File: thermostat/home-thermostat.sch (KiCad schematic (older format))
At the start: 53 parts, among them J1 Amphenol_132289 SMA, J4 Conn_ARM_JTAG_SWD_10, U1 MKW41Z512VHT, U10 SN74LVC2T45DCUR, U9 SN74LVC2T45DCUR, Y1 32MHz 10PPM SMT 2.0x1.6mm 10PF, Y2 32.768KHz 20PPM 3.2x1.5mm 7PF

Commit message: Fine grouping of parts done, may start routing . GPIO connector on wrong side of PCB (I wanted to have the buttons on the opposite side, but thats not a big problem.
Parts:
- removed TP13: UART_TX, TestPoint:TestPoint_Pad_D1.0mm, symbol Connector:TestPoint
- removed TP16: UART_RX, TestPoint:TestPoint_Pad_D1.0mm, symbol Connector:TestPoint
- added J7: Thermosthat, Connector_PinHeader_2.54mm:PinHeader_1x03_P2.54mm_Vertical_SMD_Pin1Left, symbol Connector_Generic:Conn_01x03
- C14, C29, C46, C47, C48, C56, C57, C58, C59: footprint Capacitor_SMD:C_0603_1608Metric -> Capacitor_SMD:C_0402_1005Metric
- R2: footprint Resistor_SMD:R_0603_1608Metric -> Resistor_SMD:R_0402_1005Metric
- U1: footprint Package_DFN_QFN:NXP_LQFN-48-1EP_7x7mm_P0.5mm_EP3.5x3.5mm_16xMask0.45x0.45_ThermalVias -> Package_DFN_QFN:NXP_LQFN-48-1EP_7x7mm_P0.5mm_EP3.5x3.5mm_16xMask0.45x0.45
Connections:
- net BTN_OK: now also U1.41 (PTC5)
- net GND: now also J7.3 (Pin_3)
- net UART_TX: now reaches U9.7 (B1)
- net UART_TX: now also J7.1 (Pin_1)
- net UART_RX: now reaches U10.7 (B1)
- net UART_RX: now also J7.2 (Pin_2)
- no-connect marks 18 -> 17
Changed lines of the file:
@@
 F 0 "C14" H -935 1996 50  0000 L CNN
 F 1 "1n" H -935 1905 50  0000 L CNN
-F 2 "Capacitor_SMD:C_0603_1608Metric" H -1012 1800 50  0001 C CNN
+F 2 "Capacitor_SMD:C_0402_1005Metric" H -1012 1800 50  0001 C CNN
 F 3 "~" H -1050 1950 50  0001 C CNN
 	1    -1050 1950
@@
 F 0 "R2" H -1120 1404 50  0000 R CNN
 F 1 "0" H -1120 1495 50  0000 R CNN
-F 2 "Resistor_SMD:R_0603_1608Metric" V -1120 1450 50  0001 C CNN
+F 2 "Resistor_SMD:R_0402_1005Metric" V -1120 1450 50  0001 C CNN
 F 3 "~" H -1050 1450 50  0001 C CNN
 	1    -1050 1450
@@
 F1 "gpio.sch" 50
 F2 "BTN_OK" I L 12650 3400 50
-F3 "BTN_CANCEL" I L 12650 3500 50
-F4 "LED_OUT" I L 12650 3600 50
-F5 "LED_RED" I L 12650 3700 50
-F6 "LED_GREEN" I L 12650 3800 50
-F7 "SCL" I L 12650 3000 50
-F8 "SDA" I L 12650 3100 50
-F9 "~INT" I L 12650 3200 50
-F10 "BTN_RST" I L 12650 3300 50
+F3 "LED_OUT" I L 12650 3600 50
+F4 "LED_RED" I L 12650 3700 50
+F5 "LED_GREEN" I L 12650 3800 50
+F6 "SCL" I L 12650 3000 50
+F7 "SDA" I L 12650 3100 50
+F8 "~INT" I L 12650 3200 50
+F9 "BTN_RST" I L 12650 3300 50
 $EndSheet
 Text Label 8200 3150 2    50   ~ 0
@@
 Text Label 12150 3400 0    50   ~ 0
 BTN_OK
-Text Label 12150 3500 0    50   ~ 0
-BTN_CANCEL
 Wire Wire Line
 	12150 3400 12650 3400
-Wire Wire Line
-	12150 3500 12650 3500
 Wire Wire Line
 	8200 2550 7650 2550
@@
 F 0 "U1" H 6000 5800 50  0000 C CNN
 F 1 "MKW41Z512VHT" H 7600 5800 50  0000 C CNN
-F 2 "Package_DFN_QFN:NXP_LQFN-48-1EP_7x7mm_P0.5mm_EP3.5x3.5mm_16xMask0.45x0.45_ThermalVias" H 6700 4050 50  0001 C CNN
+F 2 "Package_DFN_QFN:NXP_LQFN-48-1EP_7x7mm_P0.5mm_EP3.5x3.5mm_16xMask0.45x0.45" H 6700 4050 50  0001 C CNN
 F 3 "https://www.nxp.com/docs/en/data-sheet/MKW41Z512.pdf" H 6750 3950 50  0001 C CNN
 	1    6750 4050
@@
 $EndComp
 NoConn ~ 7650 2850
-NoConn ~ 7650 2950
 NoConn ~ 7650 3350
 NoConn ~ 7650 3950
@@
 F 0 "C46" H -2135 4996 50  0000 L CNN
 F 1 "1u" H -2135 4905 50  0000 L CNN
-F 2 "Capacitor_SMD:C_0603_1608Metric" H -2212 4800 50  0001 C CNN
+F 2 "Capacitor_SMD:C_0402_1005Metric" H -2212 4800 50  0001 C CNN
 F 3 "~" H -2250 4950 50  0001 C CNN
 	1    -2250 4950
@@
 F 0 "C47" H -1035 4996 50  0000 L CNN
 F 1 "1u" H -1035 4905 50  0000 L CNN
-F 2 "Capacitor_SMD:C_0603_1608Metric" H -1112 4800 50  0001 C CNN
+F 2 "Capacitor_SMD:C_0402_1005Metric" H -1112 4800 50  0001 C CNN
 F 3 "~" H -1150 4950 50  0001 C CNN
 	1    -1150 4950
@@
 F 0 "C48" H -685 4996 50  0000 L CNN
 F 1 "0,1u" H -685 4905 50  0000 L CNN
-F 2 "Capacitor_SMD:C_0603_1608Metric" H -762 4800 50  0001 C CNN
+F 2 "Capacitor_SMD:C_0402_1005Metric" H -762 4800 50  0001 C CNN
 F 3 "~" H -800 4950 50  0001 C CNN
 	1    -800 4950
@@
 F 0 "C29" H -2535 4996 50  0000 L CNN
 F 1 "0,1u" H -2535 4905 50  0000 L CNN
-F 2 "Capacitor_SMD:C_0603_1608Metric" H -2612 4800 50  0001 C CNN
+F 2 "Capacitor_SMD:C_0402_1005Metric" H -2612 4800 50  0001 C CNN
 F 3 "~" H -2650 4950 50  0001 C CNN
 	1    -2650 4950
@@
 Wire Wire Line
 	-2750 5650 -2100 5650
-$Comp
-L Connector:TestPoint TP13
-U 1 1 5F7FA6AE
-P -1000 5650
-F 0 "TP13" V -805 5722 50  0000 C CNN
-F 1 "UART_TX" V -896 5722 50  0000 C CNN
-F 2 "TestPoint:TestPoint_Pad_D1.0mm" H -800 5650 50  0001 C CNN
-F 3 "~" H -800 5650 50  0001 C CNN
-	1    -1000 5650
-	0    1    1    0
-$EndComp
 Wire Wire Line
 	-1000 5650 -1300 5650
@@
 F 0 "C57" H -2135 7196 50  0000 L CNN
 F 1 "1u" H -2135 7105 50  0000 L CNN
-F 2 "Capacitor_SMD:C_0603_1608Metric" H -2212 7000 50  0001 C CNN
+F 2 "Capacitor_SMD:C_0402_1005Metric" H -2212 7000 50  0001 C CNN
 F 3 "~" H -2250 7150 50  0001 C CNN
 	1    -2250 7150
@@
 F 0 "C58" H -1035 7196 50  0000 L CNN
 F 1 "1u" H -1035 7105 50  0000 L CNN
-F 2 "Capacitor_SMD:C_0603_1608Metric" H -1112 7000 50  0001 C CNN
+F 2 "Capacitor_SMD:C_0402_1005Metric" H -1112 7000 50  0001 C CNN
 F 3 "~" H -1150 7150 50  0001 C CNN
 	1    -1150 7150
@@
 F 0 "C59" H -685 7196 50  0000 L CNN
 F 1 "0,1u" H -685 7105 50  0000 L CNN
-F 2 "Capacitor_SMD:C_0603_1608Metric" H -762 7000 50  0001 C CNN
+F 2 "Capacitor_SMD:C_0402_1005Metric" H -762 7000 50  0001 C CNN
 F 3 "~" H -800 7150 50  0001 C CNN
 	1    -800 7150
@@
 F 0 "C56" H -2535 7196 50  0000 L CNN
 F 1 "0,1u" H -2535 7105 50  0000 L CNN
-F 2 "Capacitor_SMD:C_0603_1608Metric" H -2612 7000 50  0001 C CNN
+F 2 "Capacitor_SMD:C_0402_1005Metric" H -2612 7000 50  0001 C CNN
 F 3 "~" H -2650 7150 50  0001 C CNN
 	1    -2650 7150
@@
 	-350 6950 -800 6950
 Connection ~ -800 6950
-$Comp
-L Connector:TestPoint TP16
-U 1 1 5F8612B7
-P -1000 7850
-F 0 "TP16" V -805 7922 50  0000 C CNN
-F 1 "UART_RX" V -896 7922 50  0000 C CNN
-F 2 "TestPoint:TestPoint_Pad_D1.0mm" H -800 7850 50  0001 C CNN
-F 3 "~" H -800 7850 50  0001 C CNN
-	1    -1000 7850
-	0    1    1    0
-$EndComp
 Wire Wire Line
 	-1800 6950 -1800 7450
@@
 	-1050 1750 -1050 1800
 Connection ~ -1050 1750
+$Comp
+L Connector_Generic:Conn_01x03 J7
+U 1 1 5FA1C616
+P 1600 6900
+AR Path="/5FA1C616" Ref="J7"  Part="1"
+AR Path="/5E6A63AE/5FA1C616" Ref="J?"  Part="1"
+F 0 "J7" H 1680 6942 50  0000 L CNN
+F 1 "Thermosthat" H 1680 6851 50  0000 L CNN
+F 2 "Connector_PinHeader_2.54mm:PinHeader_1x03_P2.54mm_Vertical_SMD_Pin1Left" H 1600 6900 50  0001 C CNN
+F 3 "~" H 1600 6900 50  0001 C CNN
+	1    1600 6900
+	1    0    0    -1
+$EndComp
+Text Label -1000 5650 2    50   ~ 0
+UART_TX
+Text Label -1000 7850 2    50   ~ 0
+UART_RX
+$Comp
+L power:GND #PWR?
+U 1 1 5FA2E08F
+P 1350 7050
+AR Path="/5E8AC4D3/5FA2E08F" Ref="#PWR?"  Part="1"
+AR Path="/5FA2E08F" Ref="#PWR0114"  Part="1"
+F 0 "#PWR0114" H 1350 6800 50  0001 C CNN
+F 1 "GND" H 1355 6877 50  0000 C CNN
+F 2 "" H 1350 7050 50  0001 C CNN
+F 3 "" H 1350 7050 50  0001 C CNN
+	1    1350 7050
+	1    0    0    -1
+$EndComp
+Wire Wire Line
+	1350 7050 1350 7000
+Wire Wire Line
+	1350 7000 1400 7000
+Text Label 1050 6900 0    50   ~ 0
+UART_RX
+Text Label 1050 6800 0    50   ~ 0
+UART_TX
+Wire Wire Line
+	1050 6800 1400 6800
+Wire Wire Line
+	1050 6900 1400 6900
+Text Label 8200 2950 2    50   ~ 0
+BTN_OK
+Wire Wire Line
+	8200 2950 7650 2950
 $EndSCHEMATC

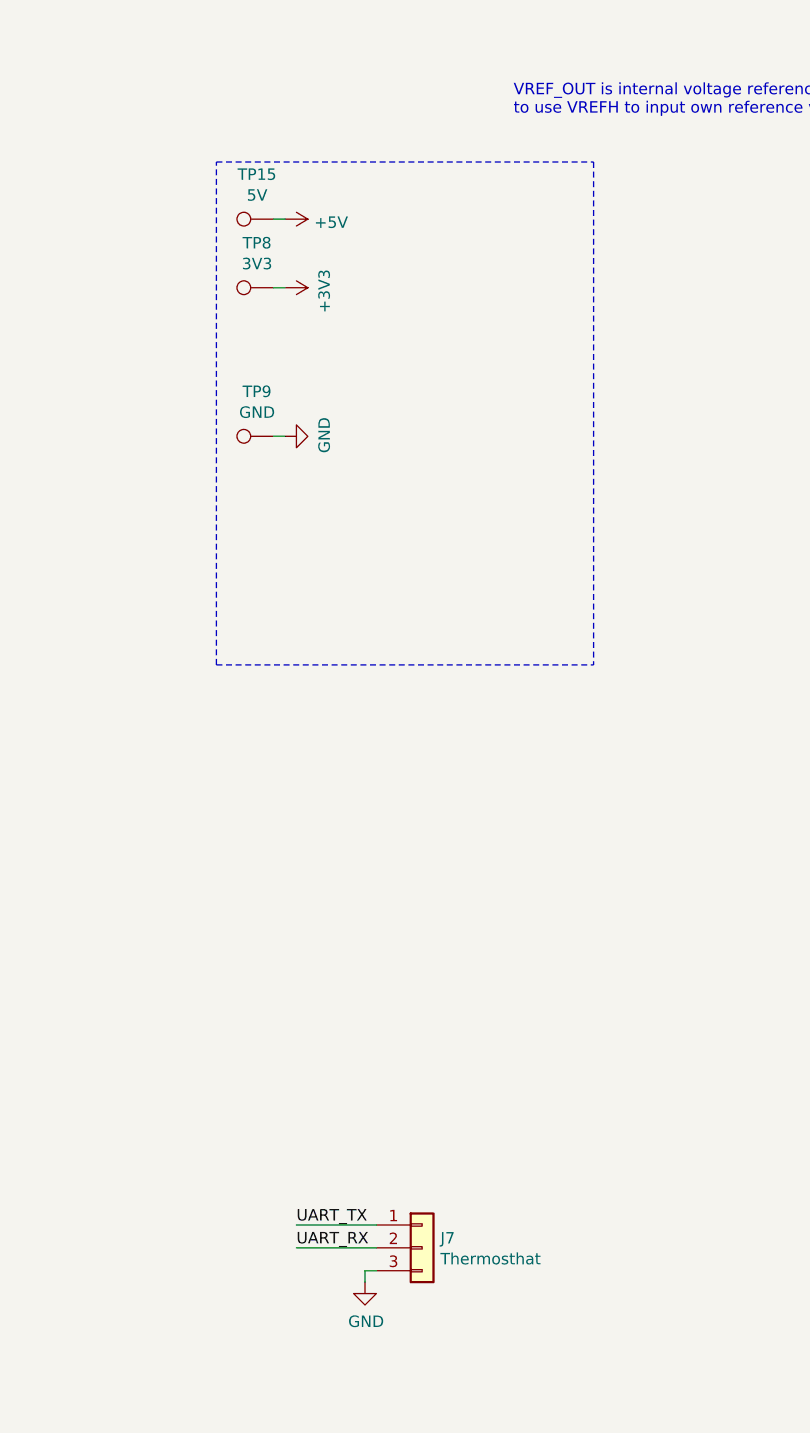
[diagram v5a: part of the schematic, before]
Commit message: Changed LED and regulator_out drivers to NMOS instead of bipolar. Started routing, SPI and I2C lines done.
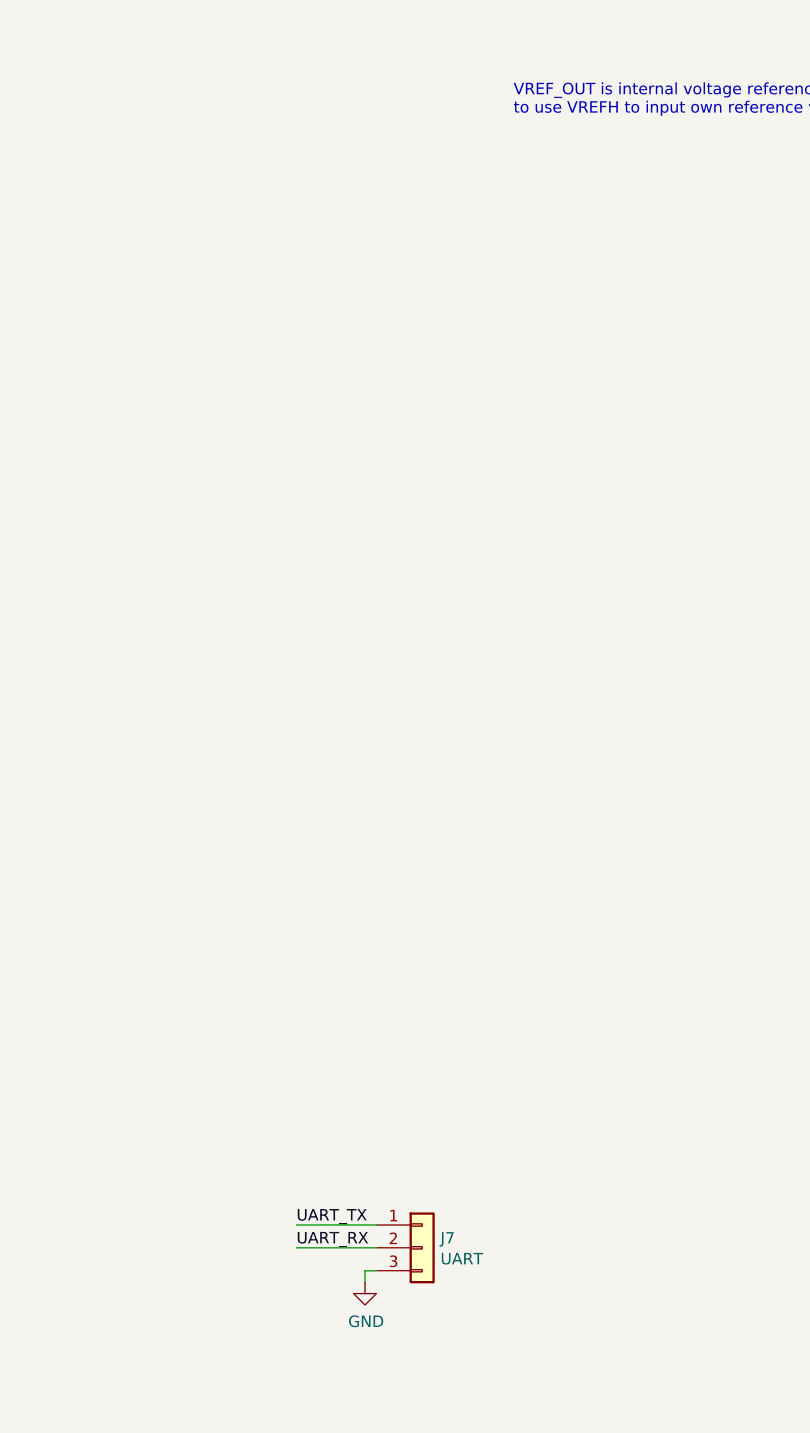
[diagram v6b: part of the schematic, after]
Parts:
- removed TP15: 5V, TestPoint:TestPoint_Pad_D1.0mm, symbol Connector:TestPoint
- removed TP8: 3V3, TestPoint:TestPoint_Pad_D1.0mm, symbol Connector:TestPoint
- removed TP9: GND, TestPoint:TestPoint_Pad_D1.0mm, symbol Connector:TestPoint
- J7: value Thermosthat -> UART
- U1: footprint Package_DFN_QFN:NXP_LQFN-48-1EP_7x7mm_P0.5mm_EP3.5x3.5mm_16xMask0.45x0.45 -> Package_DFN_QFN:NXP_LQFN-48-1EP_7x7mm_P0.5mm_EP3.5x3.5mm_16xMask0.45x0.45_ThermalVias
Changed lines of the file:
@@
 Wire Wire Line
 	-1050 1250 -1050 1300
-Wire Notes Line
-	700  4350 700  2150
-Wire Notes Line
-	700  2150 2350 2150
-Wire Notes Line
-	2350 2150 2350 4350
-Wire Notes Line
-	700  4350 2350 4350
 $Comp
 L Connector:Conn_Coaxial J1
@@
 Text Notes 7850 6300 0    50   ~ 0
 This matching network transform device impedance to 50Ohms\nPlace as close to device as possible
-$Comp
-L Connector:TestPoint TP9
-U 1 1 5F554204
-P 950 3350
-F 0 "TP9" V 1145 3422 50  0000 C CNN
-F 1 "GND" V 1054 3422 50  0000 C CNN
-F 2 "TestPoint:TestPoint_Pad_D1.0mm" H 1150 3350 50  0001 C CNN
-F 3 "~" H 1150 3350 50  0001 C CNN
-	1    950  3350
-	0    -1   -1   0
-$EndComp
-$Comp
-L power:GND #PWR?
-U 1 1 5F5544E3
-P 1000 3350
-AR Path="/5E8AC4D3/5F5544E3" Ref="#PWR?"  Part="1"
-AR Path="/5F5544E3" Ref="#PWR016"  Part="1"
-F 0 "#PWR016" H 1000 3100 50  0001 C CNN
-F 1 "GND" H 1005 3177 50  0000 C CNN
-F 2 "" H 1000 3350 50  0001 C CNN
-F 3 "" H 1000 3350 50  0001 C CNN
-	1    1000 3350
-	0    -1   -1   0
-$EndComp
-Wire Wire Line
-	1000 3350 950  3350
-$Comp
-L power:+3V3 #PWR?
-U 1 1 5F55E07F
-P 1000 2700
-AR Path="/5E8AC4D3/5F55E07F" Ref="#PWR?"  Part="1"
-AR Path="/5F55E07F" Ref="#PWR015"  Part="1"
-F 0 "#PWR015" H 1000 2550 50  0001 C CNN
-F 1 "+3V3" H 1015 2873 50  0000 C CNN
-F 2 "" H 1000 2700 50  0001 C CNN
-F 3 "" H 1000 2700 50  0001 C CNN
-	1    1000 2700
-	0    1    1    0
-$EndComp
-$Comp
-L Connector:TestPoint TP8
-U 1 1 5F55EE65
-P 950 2700
-F 0 "TP8" V 1145 2772 50  0000 C CNN
-F 1 "3V3" V 1054 2772 50  0000 C CNN
-F 2 "TestPoint:TestPoint_Pad_D1.0mm" H 1150 2700 50  0001 C CNN
-F 3 "~" H 1150 2700 50  0001 C CNN
-	1    950  2700
-	0    -1   -1   0
-$EndComp
-Wire Wire Line
-	950  2700 1000 2700
 Text Label 8200 5050 2    50   ~ 0
 SPI1_SCK
@@
 F 0 "U1" H 6000 5800 50  0000 C CNN
 F 1 "MKW41Z512VHT" H 7600 5800 50  0000 C CNN
-F 2 "Package_DFN_QFN:NXP_LQFN-48-1EP_7x7mm_P0.5mm_EP3.5x3.5mm_16xMask0.45x0.45" H 6700 4050 50  0001 C CNN
+F 2 "Package_DFN_QFN:NXP_LQFN-48-1EP_7x7mm_P0.5mm_EP3.5x3.5mm_16xMask0.45x0.45_ThermalVias" H 6700 4050 50  0001 C CNN
 F 3 "https://www.nxp.com/docs/en/data-sheet/MKW41Z512.pdf" H 6750 3950 50  0001 C CNN
 	1    6750 4050
@@
 	5450 3950 5850 3950
 $Comp
-L Connector:TestPoint TP15
-U 1 1 5F6F1851
-P 950 2400
-F 0 "TP15" V 1145 2472 50  0000 C CNN
-F 1 "5V" V 1054 2472 50  0000 C CNN
-F 2 "TestPoint:TestPoint_Pad_D1.0mm" H 1150 2400 50  0001 C CNN
-F 3 "~" H 1150 2400 50  0001 C CNN
-	1    950  2400
-	0    -1   -1   0
-$EndComp
-$Comp
-L power:+5V #PWR096
-U 1 1 5F6F2232
-P 1000 2400
-F 0 "#PWR096" H 1000 2250 50  0001 C CNN
-F 1 "+5V" V 1015 2528 50  0000 L CNN
-F 2 "" H 1000 2400 50  0001 C CNN
-F 3 "" H 1000 2400 50  0001 C CNN
-	1    1000 2400
-	0    1    1    0
-$EndComp
-Wire Wire Line
-	1000 2400 950  2400
-$Comp
 L Device:L L6
 U 1 1 5F711776
@@
 AR Path="/5E6A63AE/5FA1C616" Ref="J?"  Part="1"
 F 0 "J7" H 1680 6942 50  0000 L CNN
-F 1 "Thermosthat" H 1680 6851 50  0000 L CNN
+F 1 "UART" H 1680 6851 50  0000 L CNN
 F 2 "Connector_PinHeader_2.54mm:PinHeader_1x03_P2.54mm_Vertical_SMD_Pin1Left" H 1600 6900 50  0001 C CNN
 F 3 "~" H 1600 6900 50  0001 C CNN
